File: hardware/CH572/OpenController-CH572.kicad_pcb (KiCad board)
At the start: 2 copper layers, 10 x 20.5 mm, 9 parts, among them J1 Castellated, U1 CH572D, U2 XC6206P332MR-G, Y1 32MHz

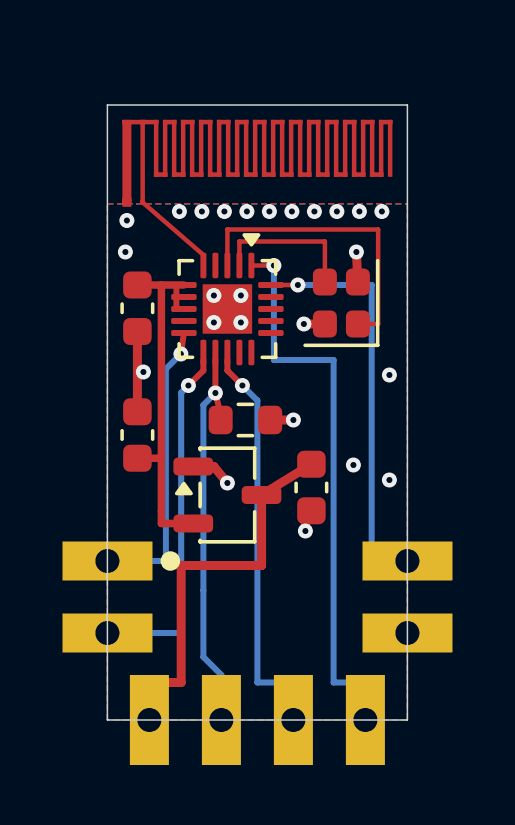
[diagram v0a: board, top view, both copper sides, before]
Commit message: hardware: move the CH572 castellations to a 0.1 in grid
Nine castellated half-holes (1.0 mm drill, 1.5 x 3.0 mm pads) replace the
eight on a 2.4 mm pitch: three on each side and three on the end opposite
the antenna, all on one 0.1 in grid so a host can also take standard pin
headers. The board widens from 10.0 mm to 10.16 mm so the side rows sit
0.4 in apart; the antenna stays centred. Viewed from the top with the
antenna at the bottom, the pads count counter-clockwise from the
top-left: 1 GND, 2 UART_TX, 3 UART_RX, 4 NRST, 5 VCC, 6 GND, 7 SWDIO,
8 SWCLK, 9 WAKE.

The board is now drawn with the antenna at the bottom (rotated 180
degrees). Besides the new J1 footprint and the wider outline and pours,
the layout change re-points the six bottom-layer castellation runs and
the VCC run, moves C2 0.6 mm with its two tracks, moves two ground vias
clear of the new pads and adds two stitching vias beside the ground
castellations. The RF area is unchanged.

The outermost holes sit 2.54 mm from the corners, which clears
JLCPCB's 1 mm castellated-pad-to-edge rule under both its English (pad
edge) and Chinese (hole edge) wording. Only the 3 mm hole-to-corner row
in the English design guide's expanded table is not met; the README
records why. ERC and DRC (with schematic parity) report no violations.

Co-Authored-By: Claude Opus 5.5 <noreply@anthropic.com>
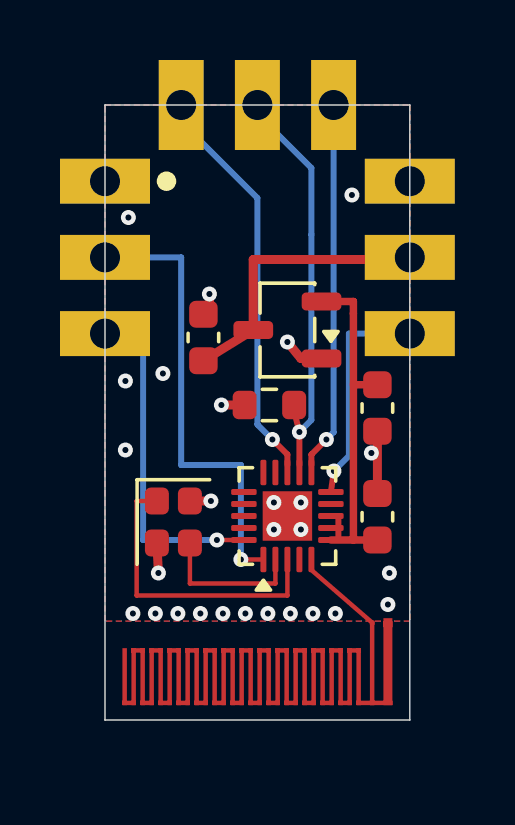
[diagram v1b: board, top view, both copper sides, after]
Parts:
- J1: footprint OpenController:Castellated_CH572_10x20.5mm -> OpenController:Castellated_CH572_10.16x20.5mm
- moved J1 20.5 mm to (99.9, 100.0)
- moved AE1 16.6 mm to (105.0, 118.5), turned to 180 degrees
- moved C3 10.6 mm to (109.0, 113.7), turned to 90 degrees
- moved Y1 9.20 mm to (102.2, 113.9), turned to -90 degrees
- moved C2 8.05 mm to (109.0, 110.1), turned to -90 degrees
- moved U1 7.18 mm to (106.0, 113.7), turned to 90 degrees
- moved C1 6.16 mm to (103.2, 107.8), turned to 90 degrees
- moved U2 5.85 mm to (106.0, 107.5), turned to 180 degrees
- moved R1 0.94 mm to (105.4, 110.0), turned to 180 degrees
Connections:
- J1 pad 1: /NRST -> GND
- J1 pad 2: /SWDIO -> /UART_TX
- J1 pad 3: VCC -> /UART_RX
- J1 pad 4: /SWCLK -> /NRST
- J1 pad 5: /WAKE -> VCC
- J1 pad 6: /UART_TX -> GND
- J1 pad 7: GND -> /SWDIO
- J1 pad 8: /UART_RX -> /SWCLK
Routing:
- net VCC: track 11.9 -> 8.74 mm
- net /UART_TX: track 17.7 -> 14.7 mm
- net /NRST: track 9.01 -> 6.74 mm
- net /UART_RX: track 12.6 -> 10.8 mm
- net GND: track 7.42 -> 6.82 mm, vias 25 -> 27
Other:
- board size 10 x 20.5 mm -> 10.2 x 20.5 mm

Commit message: hardware: keep the CH572 exposed-pad paste off its thermal vias
The exposed pad's four 0.2 mm GND vias sat inside the footprint's 2 x 2
paste windows, so solder could wick into the open barrels during reflow
and starve the CH572D's only ground connection (CodeRabbit review).

U1 now uses a project copy of KiCad's QFN-20-1EP_3x3mm_P0.4mm_EP1.65x1.65mm
land pattern with four 0.4/0.2 mm thermal vias built in, 0.6 mm from the
centre along each axis. The paste is a central window plus four edge
windows covering about 47% of the pad, each at least 0.1 mm clear of the
via copper. The separate board vias in the pad are gone. ERC and DRC
(with schematic parity) report no violations.

Co-Authored-By: Claude Opus 5.5 <noreply@anthropic.com>
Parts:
- U1: footprint Package_DFN_QFN:QFN-20-1EP_3x3mm_P0.4mm_EP1.65x1.65mm -> OpenController:QFN-20-1EP_3x3mm_P0.4mm_EP1.65x1.65mm_ThermalVias
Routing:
- net GND: vias 27 -> 23

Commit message: hardware: draw the CH572D QFN footprint for OpenController
U1's thermal-via footprint was a modified copy of KiCad's
QFN-20-1EP_3x3mm_P0.4mm_EP1.65x1.65mm. KiCad's libraries are CC-BY-SA
4.0, and their exception does not cover library parts redistributed as
separate files, so that copy could not sit in a CERN-OHL-W project
library (Codex review).

The new footprint is drawn from scratch from the CH572 datasheet's QFN20
drawing (3.0 +/- 0.1 mm body, 1.8 +/- 0.2 mm exposed pad, 0.35 +/- 0.12
mm leads):
- lands 1.15 to 1.85 mm from the centre, 0.15 mm clear of the largest
  exposed pad;
- a 1.8 mm exposed-pad land with four 0.4/0.2 mm tented thermal vias at
  (+/-0.65, +/-0.65) mm;
- exposed-pad paste in a centre window plus four edge windows, 51% of
  the pad with their rounded corners and at least 0.09 mm clear of the
  via copper.
hardware/NOTICE records the footprint's provenance.

The README now quotes paste coverage including the windows' rounded
corners, and names the thermal vias (1.1 mm apart) rather than the
castellations as the closest plated pad holes. ERC and DRC (with
schematic parity) report no violations.

Co-Authored-By: Claude Opus 5.5 <noreply@anthropic.com>
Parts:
- U1: footprint OpenController:QFN-20-1EP_3x3mm_P0.4mm_EP1.65x1.65mm_ThermalVias -> OpenController:CH572D_QFN-20_3x3mm_P0.4mm_EP1.8mm_ThermalVias
